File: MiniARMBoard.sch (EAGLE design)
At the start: 37 parts, among them CN1 J_USB_MICROAB_HIROSE_ZX62-AB-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, U1 LPC1549JBD48, U2 FT232RQ, U3 MCP1700T-33, U4 ADR5041, X1 FA238V

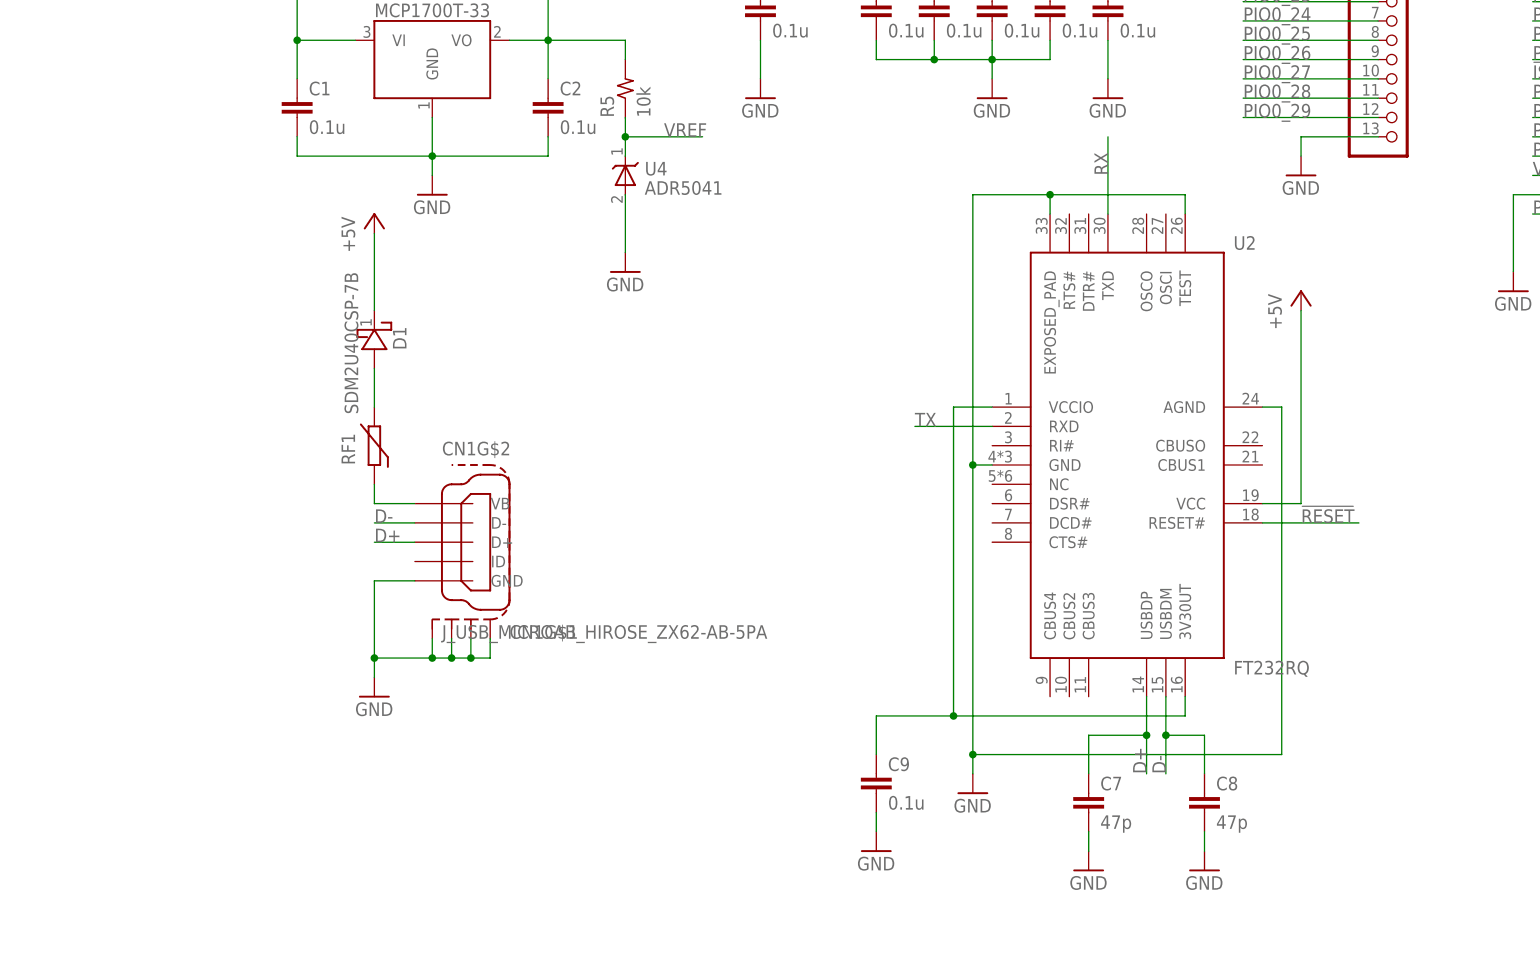
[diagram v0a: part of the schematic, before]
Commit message: パーツ変更
USBの保護をRFからICに
シリアル変換ICをFT234XDに
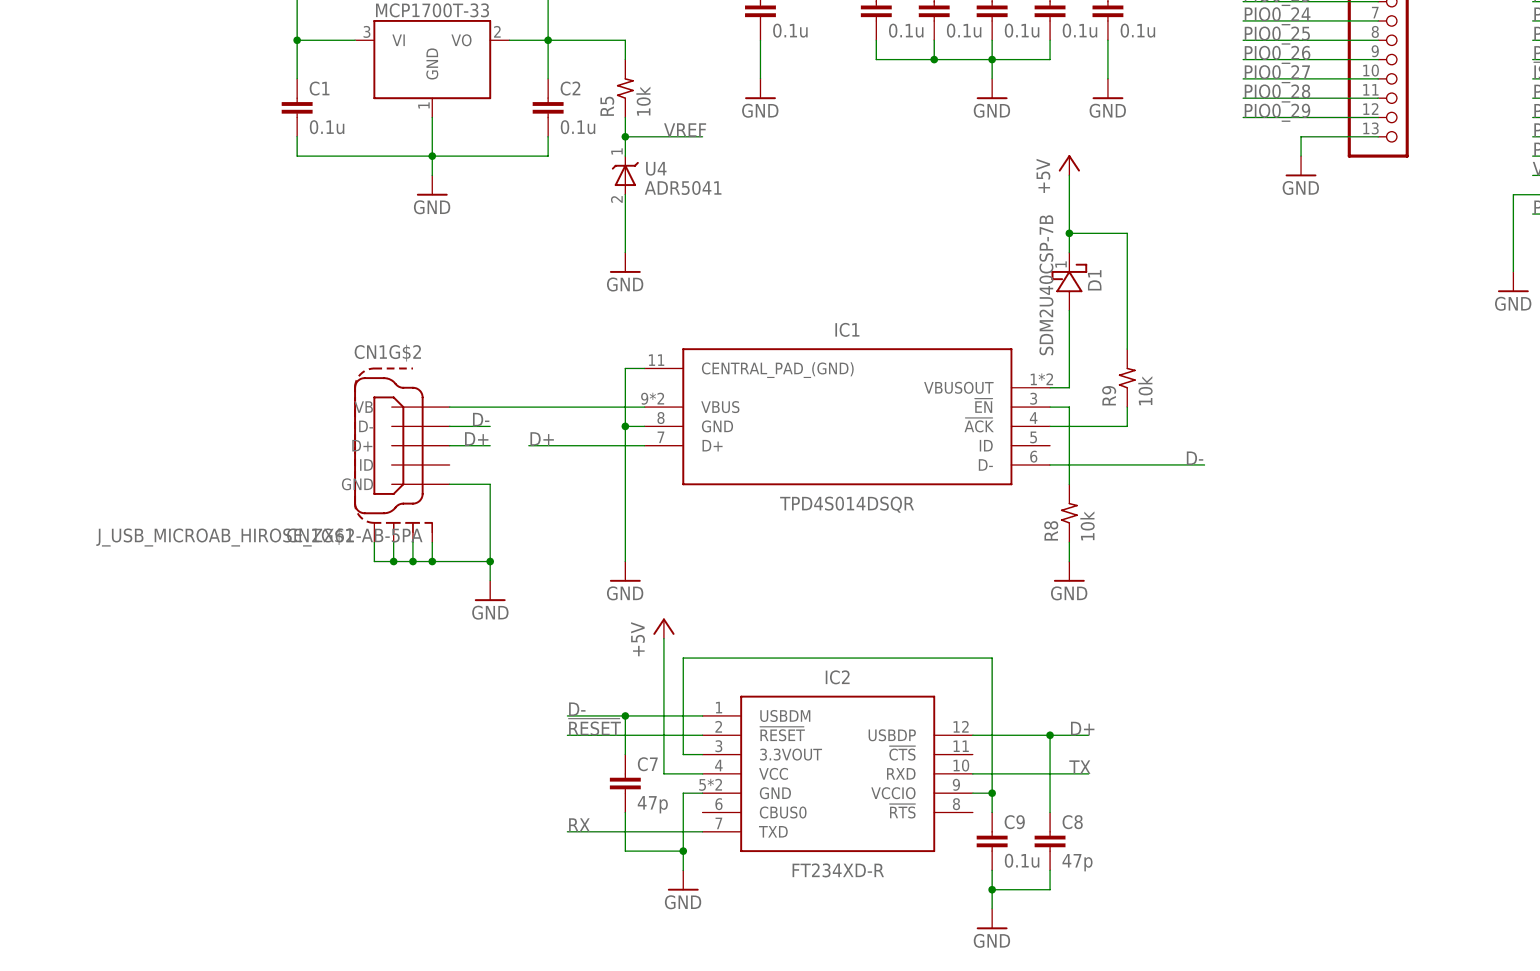
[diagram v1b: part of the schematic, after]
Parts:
- removed RF1: (no value), Passive:RF1608
- removed U2: FT232RQ, FT232RQ:FT232RQ
- added IC1: TPD4S014DSQR, TPD4S014DSQR:TPD4S014DSQR
- added IC2: FT234XD-R, FT234XD-R:FT234XD-R
- added R8, R9: 10k, MotorDriver:R1005
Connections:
- removed net N$11: C9.1, U2.3V30UT, U2.VCCIO
- new net N$4: C9.1, IC2.3.3VOUT, IC2.VCCIO
- new net N$6: IC1.!EN, R8.2
- new net N$7: IC1.!ACK, R9.1
- net !RESET: now also IC2.!RESET; no longer U2.RESET#
- net +5V: now also IC2.VCC, R9.2; no longer U2.VCC
- net D+: now also C8.1, IC1.D+, IC2.USBDP; no longer C7.1, U2.USBDP
- net D-: now also C7.1, IC1.D-, IC2.USBDM; no longer C8.1, U2.USBDM
- net GND: now also IC1.CENTRAL_PAD_(GND), IC1.GND, IC2.GND, R8.1; no longer U2.AGND, U2.EXPOSED_PAD, U2.GND, U2.TEST
- net N$3: now also IC1.VBUSOUT; no longer RF1.2
- net N$56: now also IC1.VBUS; no longer RF1.1
- net RX: now also IC2.TXD; no longer U2.TXD
- net TX: now also IC2.RXD; no longer U2.RXD
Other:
- moved on the sheet: C7, C8, C9, CN1G$1, CN1G$2, D1

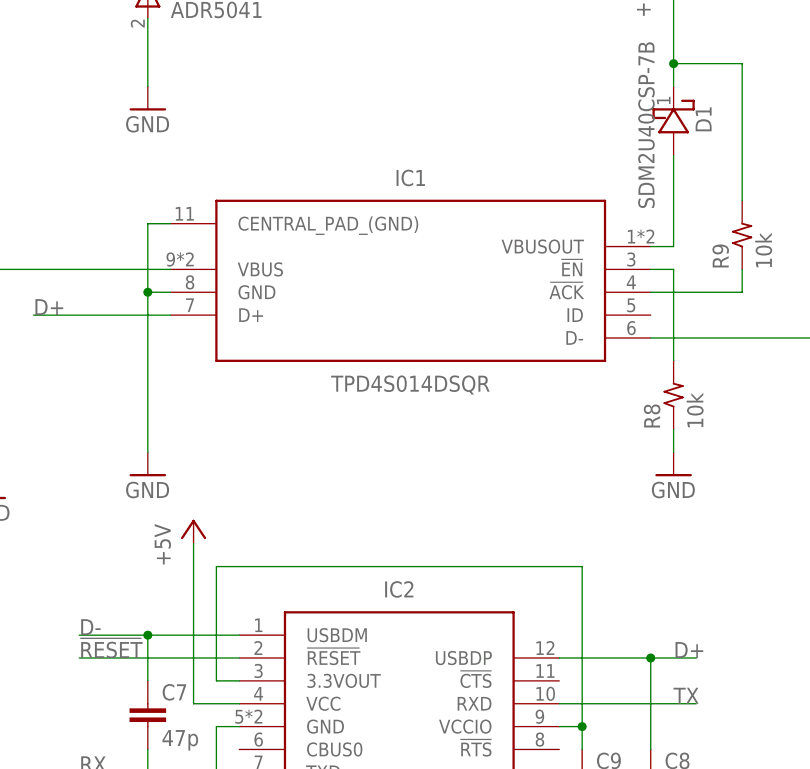
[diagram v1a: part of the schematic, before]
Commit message: ICの名前を'IC*'から'U*'に変更
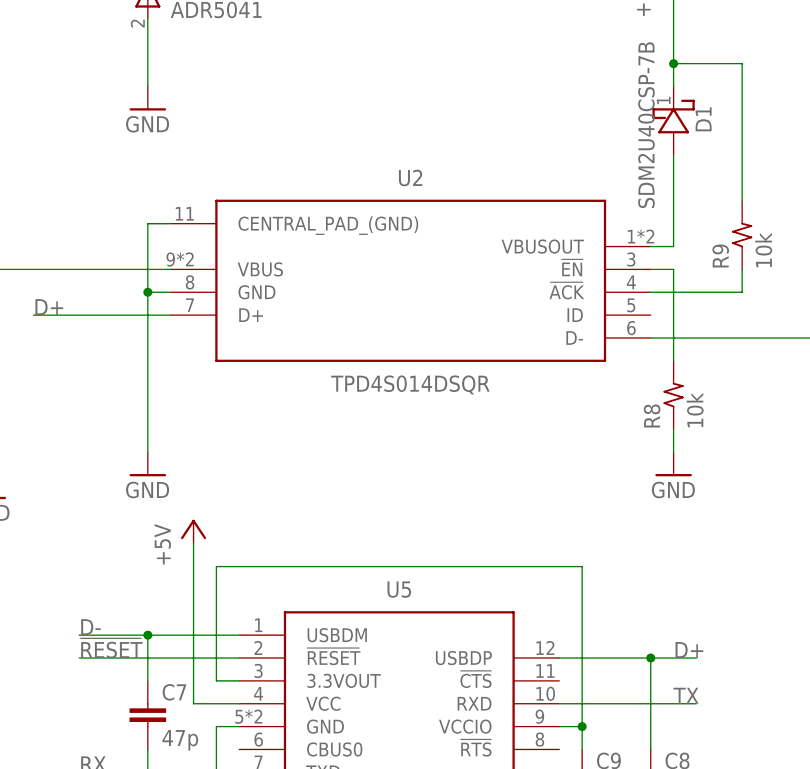
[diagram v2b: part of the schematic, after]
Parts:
- renumbered IC1 to U2, IC2 to U5
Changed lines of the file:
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@@
 <?xml version="1.0" encoding="utf-8"?>
 <!DOCTYPE eagle SYSTEM "eagle.dtd">
-<eagle version="8.4.1">
+<eagle version="8.4.3">
 <drawing>
 <settings>
@@
 <part name="CN2" library="nonolith" library_urn="urn:adsk.eagle:library:1289076" deviceset="HEADER-1X13" device="" package3d_urn="urn:adsk.eagle:package:1289318/2"/>
 <part name="CN3" library="nonolith" library_urn="urn:adsk.eagle:library:1289076" deviceset="HEADER-1X13" device="" package3d_urn="urn:adsk.eagle:package:1289318/2"/>
-<part name="IC1" library="TPD4S014DSQR" library_urn="urn:adsk.eagle:library:1437167" deviceset="TPD4S014DSQR" device="" package3d_urn="urn:adsk.eagle:package:1437170/3"/>
-<part name="IC2" library="FT234XD-R" library_urn="urn:adsk.eagle:library:1437157" deviceset="FT234XD-R" device="" package3d_urn="urn:adsk.eagle:package:1437160/3"/>
+<part name="U2" library="TPD4S014DSQR" library_urn="urn:adsk.eagle:library:1437167" deviceset="TPD4S014DSQR" device="" package3d_urn="urn:adsk.eagle:package:1437170/3"/>
+<part name="U5" library="FT234XD-R" library_urn="urn:adsk.eagle:library:1437157" deviceset="FT234XD-R" device="" package3d_urn="urn:adsk.eagle:package:1437160/3"/>
 <part name="GND8" library="MotorDriver" library_urn="urn:adsk.eagle:library:1073580" deviceset="GND" device=""/>
 <part name="+P4" library="MotorDriver" library_urn="urn:adsk.eagle:library:1073580" deviceset="+5V" device=""/>
@@
 <instance part="CN2" gate="G$1" x="152.4" y="139.7"/>
 <instance part="CN3" gate="G$1" x="152.4" y="91.44"/>
-<instance part="IC1" gate="G$1" x="106.68" y="45.72" rot="MR0"/>
-<instance part="IC2" gate="G$1" x="60.96" y="0"/>
+<instance part="U2" gate="G$1" x="106.68" y="45.72" rot="MR0"/>
+<instance part="U5" gate="G$1" x="60.96" y="0"/>
 <instance part="GND8" gate="1" x="58.42" y="-22.86"/>
 <instance part="+P4" gate="1" x="55.88" y="12.7"/>
@@
 </segment>
 <segment>
-<pinref part="IC2" gate="G$1" pin="GND"/>
+<pinref part="U5" gate="G$1" pin="GND"/>
 <wire x1="60.96" y1="-10.16" x2="58.42" y2="-10.16" width="0.1524" layer="91"/>
 <wire x1="58.42" y1="-10.16" x2="58.42" y2="-17.78" width="0.1524" layer="91"/>
@@
 </segment>
 <segment>
-<pinref part="IC1" gate="G$1" pin="GND"/>
+<pinref part="U2" gate="G$1" pin="GND"/>
 <wire x1="53.34" y1="38.1" x2="50.8" y2="38.1" width="0.1524" layer="91"/>
 <wire x1="50.8" y1="38.1" x2="50.8" y2="20.32" width="0.1524" layer="91"/>
-<pinref part="IC1" gate="G$1" pin="CENTRAL_PAD_(GND)"/>
+<pinref part="U2" gate="G$1" pin="CENTRAL_PAD_(GND)"/>
 <wire x1="53.34" y1="45.72" x2="50.8" y2="45.72" width="0.1524" layer="91"/>
 <wire x1="50.8" y1="45.72" x2="50.8" y2="38.1" width="0.1524" layer="91"/>
@@
 </segment>
 <segment>
-<pinref part="IC2" gate="G$1" pin="VCC"/>
+<pinref part="U5" gate="G$1" pin="VCC"/>
 <wire x1="60.96" y1="-7.62" x2="55.88" y2="-7.62" width="0.1524" layer="91"/>
 <wire x1="55.88" y1="-7.62" x2="55.88" y2="10.16" width="0.1524" layer="91"/>
@@
 <segment>
 <pinref part="CN1" gate="G$2" pin="VB"/>
-<pinref part="IC1" gate="G$1" pin="VBUS"/>
+<pinref part="U2" gate="G$1" pin="VBUS"/>
 <wire x1="27.686" y1="40.64" x2="53.34" y2="40.64" width="0.1524" layer="91"/>
 </segment>
@@
 </segment>
 <segment>
-<pinref part="IC2" gate="G$1" pin="USBDM"/>
+<pinref part="U5" gate="G$1" pin="USBDM"/>
 <wire x1="60.96" y1="0" x2="50.8" y2="0" width="0.1524" layer="91"/>
 <label x="43.18" y="0" size="1.778" layer="95"/>
@@
 </segment>
 <segment>
-<pinref part="IC1" gate="G$1" pin="D-"/>
+<pinref part="U2" gate="G$1" pin="D-"/>
 <wire x1="106.68" y1="33.02" x2="127" y2="33.02" width="0.1524" layer="91"/>
 <label x="124.46" y="33.02" size="1.778" layer="95"/>
@@
 </segment>
 <segment>
-<pinref part="IC2" gate="G$1" pin="USBDP"/>
+<pinref part="U5" gate="G$1" pin="USBDP"/>
 <wire x1="96.52" y1="-2.54" x2="106.68" y2="-2.54" width="0.1524" layer="91"/>
 <label x="109.22" y="-2.54" size="1.778" layer="95"/>
@@
 </segment>
 <segment>
-<pinref part="IC1" gate="G$1" pin="D+"/>
+<pinref part="U2" gate="G$1" pin="D+"/>
 <wire x1="53.34" y1="35.56" x2="38.1" y2="35.56" width="0.1524" layer="91"/>
 <label x="38.1" y="35.56" size="1.778" layer="95"/>
@@
 </segment>
 <segment>
-<pinref part="IC2" gate="G$1" pin="TXD"/>
+<pinref part="U5" gate="G$1" pin="TXD"/>
 <wire x1="60.96" y1="-15.24" x2="43.18" y2="-15.24" width="0.1524" layer="91"/>
 <label x="43.18" y="-15.24" size="1.778" layer="95"/>
@@
 </segment>
 <segment>
-<pinref part="IC2" gate="G$1" pin="RXD"/>
+<pinref part="U5" gate="G$1" pin="RXD"/>
 <wire x1="96.52" y1="-7.62" x2="111.76" y2="-7.62" width="0.1524" layer="91"/>
 <label x="109.22" y="-7.62" size="1.778" layer="95"/>
@@
 </segment>
 <segment>
-<pinref part="IC2" gate="G$1" pin="!RESET"/>
+<pinref part="U5" gate="G$1" pin="!RESET"/>
 <wire x1="60.96" y1="-2.54" x2="43.18" y2="-2.54" width="0.1524" layer="91"/>
 <label x="43.18" y="-2.54" size="1.778" layer="95"/>
@@
 <segment>
 <pinref part="D1" gate="G$1" pin="A"/>
-<pinref part="IC1" gate="G$1" pin="VBUSOUT"/>
+<pinref part="U2" gate="G$1" pin="VBUSOUT"/>
 <wire x1="106.68" y1="43.18" x2="109.22" y2="43.18" width="0.1524" layer="91"/>
 <wire x1="109.22" y1="43.18" x2="109.22" y2="53.34" width="0.1524" layer="91"/>
@@
 <net name="N$4" class="0">
 <segment>
-<pinref part="IC2" gate="G$1" pin="VCCIO"/>
+<pinref part="U5" gate="G$1" pin="VCCIO"/>
 <wire x1="96.52" y1="-10.16" x2="99.06" y2="-10.16" width="0.1524" layer="91"/>
 <wire x1="99.06" y1="-10.16" x2="99.06" y2="7.62" width="0.1524" layer="91"/>
 <wire x1="99.06" y1="7.62" x2="58.42" y2="7.62" width="0.1524" layer="91"/>
 <wire x1="58.42" y1="7.62" x2="58.42" y2="-5.08" width="0.1524" layer="91"/>
-<pinref part="IC2" gate="G$1" pin="3.3VOUT"/>
+<pinref part="U5" gate="G$1" pin="3.3VOUT"/>
 <wire x1="58.42" y1="-5.08" x2="60.96" y2="-5.08" width="0.1524" layer="91"/>
 <pinref part="C9" gate="G$1" pin="1"/>
@@
 <net name="N$6" class="0">
 <segment>
-<pinref part="IC1" gate="G$1" pin="!EN"/>
+<pinref part="U2" gate="G$1" pin="!EN"/>
 <wire x1="106.68" y1="40.64" x2="109.22" y2="40.64" width="0.1524" layer="91"/>
 <wire x1="109.22" y1="40.64" x2="109.22" y2="30.48" width="0.1524" layer="91"/>
@@
 <net name="N$7" class="0">
 <segment>
-<pinref part="IC1" gate="G$1" pin="!ACK"/>
+<pinref part="U2" gate="G$1" pin="!ACK"/>
 <pinref part="R9" gate="G$1" pin="1"/>
 <wire x1="106.68" y1="38.1" x2="116.84" y2="38.1" width="0.1524" layer="91"/>

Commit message: 回路図の見た目を整えてみた
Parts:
- CN1: value J_USB_MICROAB_HIROSE_ZX62-AB-5PA -> ZX62-AB-5PA
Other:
- note added: "2018/02/10"
- note added: "Date"
- note added: "Designer"
- note added: "Keita Sekiguchi"
- note added: "LPC1549 Development Board"
- note added: "Summary"
- moved on the sheet: C1, C10, C11, C12, C13, C2, C3, C4, C5, C6, C7, C8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
